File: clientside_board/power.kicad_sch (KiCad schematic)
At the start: 11 parts, among them U3 TPS62160DGK

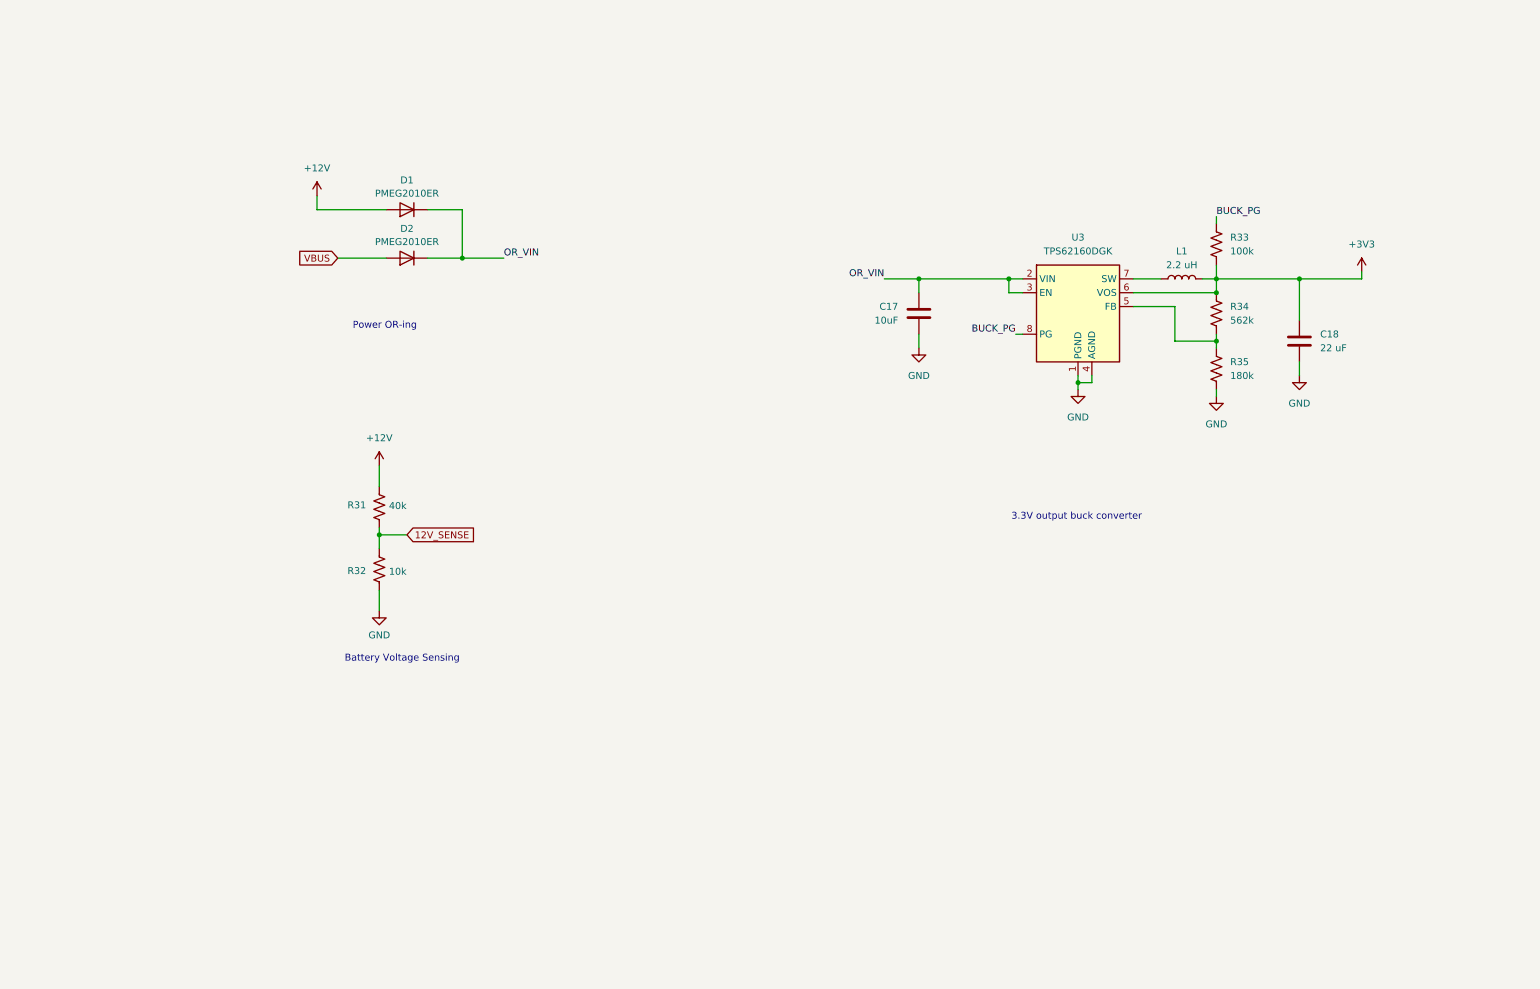
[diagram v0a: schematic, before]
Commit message: Cleanup Power and Ethernet Sheet
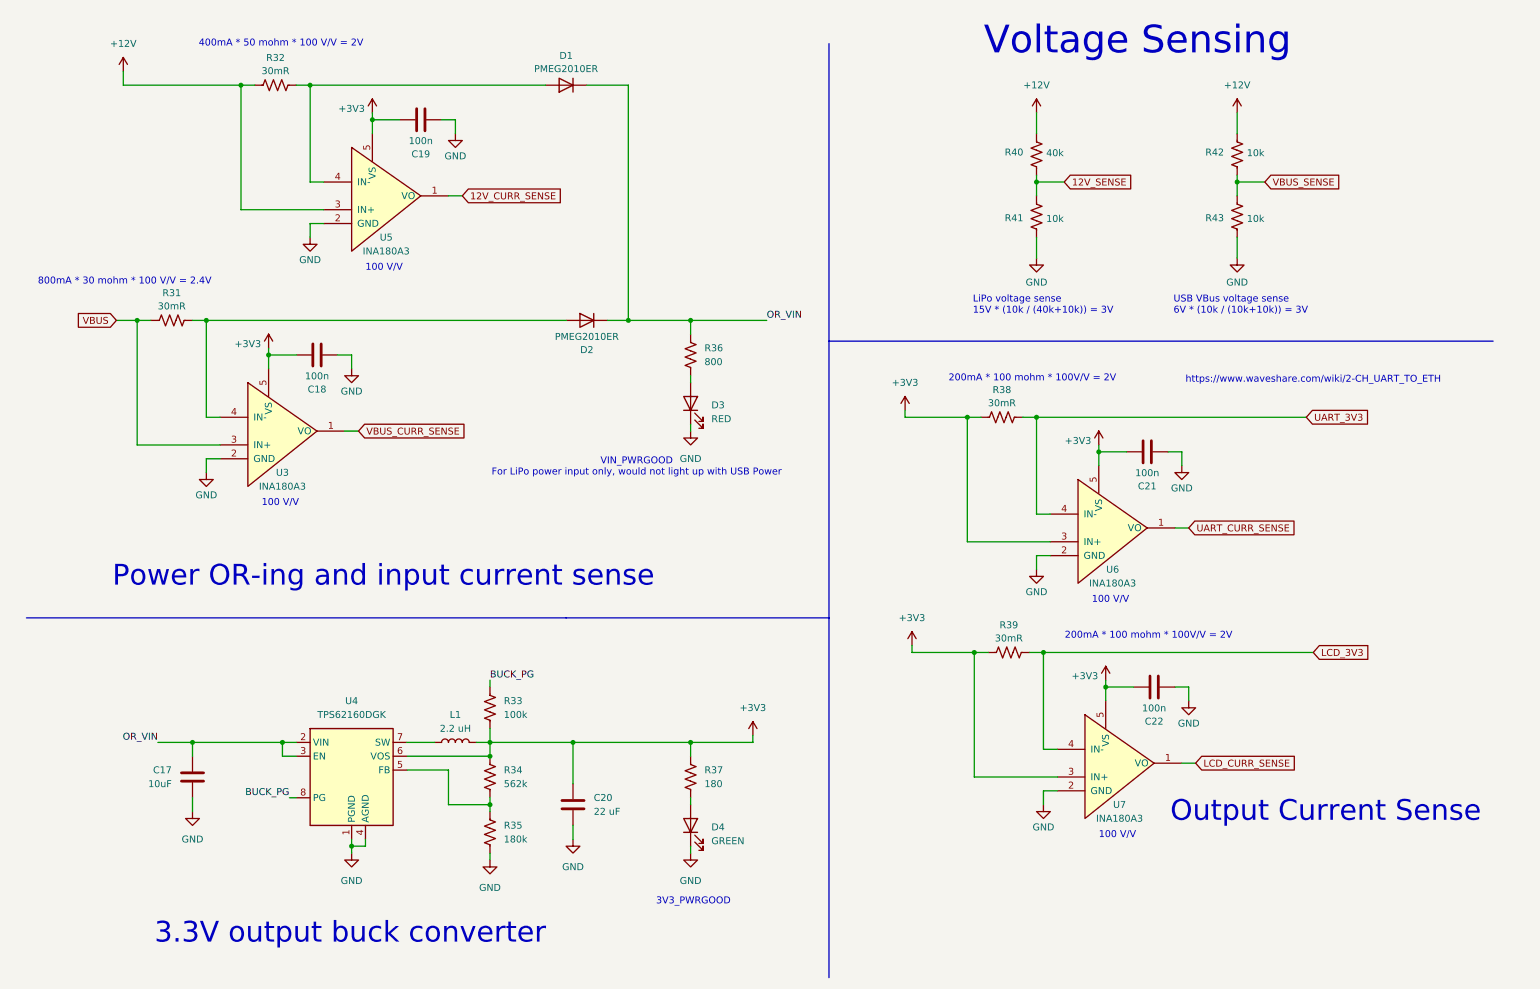
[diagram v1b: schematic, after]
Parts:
- added C18, C19, C21, C22: 100n, Capacitor_SMD:C_0805_2012Metric_Pad1.18x1.45mm_HandSolder, symbol Device:C
- added D3: RED, symbol Device:LED
- added D4: GREEN, symbol Device:LED
- added R31, R32, R38, R39: 30mR, Resistor_SMD:R_0805_2012Metric_Pad1.20x1.40mm_HandSolder, symbol Device:R_US
- added R36: 800, Resistor_SMD:R_0805_2012Metric_Pad1.20x1.40mm_HandSolder, symbol Device:R_US
- added R37: 180, Resistor_SMD:R_0805_2012Metric_Pad1.20x1.40mm_HandSolder, symbol Device:R_US
- added R42, R43: 10k, Resistor_SMD:R_0805_2012Metric_Pad1.20x1.40mm_HandSolder, symbol Device:R_US
- added U3, U5, U6, U7: INA180A3, Package_TO_SOT_SMD:SOT-23-5_HandSoldering, symbol canhw:INA180
- C17: footprint (none) -> Capacitor_SMD:C_0805_2012Metric_Pad1.18x1.45mm_HandSolder
- C20: renamed from C18; footprint (none) -> Capacitor_SMD:C_0805_2012Metric_Pad1.18x1.45mm_HandSolder
- R33, R34, R35: footprint (none) -> Resistor_SMD:R_0805_2012Metric_Pad1.20x1.40mm_HandSolder
- renumbered R31 to R40, R32 to R41, U3 to U4
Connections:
- net +12V: now also R32.1, R42.1, U5.3 (IN+); no longer D1.2 (A)
- net +3V3: now also C18.1, C19.1, C21.1, C22.1, R37.1, R38.1, R39.1, U3.5 (VS), U5.5 (VS), U6.3 (IN+), U6.5 (VS), U7.3 (IN+), U7.5 (VS)
- net GND: now also C18.2, C19.2, C21.2, C22.2, D3.1 (K), D4.1 (K), R43.2, U3.2 (GND), U5.2 (GND), U6.2 (GND), U7.2 (GND)
- net OR_VIN: now also R36.1
- net VBUS: now also R31.1, U3.3 (IN+); no longer D2.2 (A)
- new net: D2.2 (A), R31.2, U3.4 (IN-)
- new net: D3.2 (A), R36.2
- new net: D1.2 (A), R32.2, U5.4 (IN-)
- new net: D4.2 (A), R37.2
- new net 12V_CURR_SENSE: U5.1 (VO)
- new net LCD_3V3: R39.2, U7.4 (IN-)
- new net LCD_CURR_SENSE: U7.1 (VO)
- new net UART_3V3: R38.2, U6.4 (IN-)
- new net UART_CURR_SENSE: U6.1 (VO)
- new net VBUS_CURR_SENSE: U3.1 (VO)
- new net VBUS_SENSE: R42.2, R43.1
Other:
- note added: "100 V/V"
- note added: "200mA * 100 mohm * 100V/V = 2V"
- note added: "3V3_PWRGOOD"
- note added: "400mA * 50 mohm * 100 V/V = 2V"
- note added: "800mA * 30 mohm * 100 V/V = 2.4V"
- note added: "LiPo voltage sense 15V * (10k / (40k+10k)) = 3V"
- note added: "Output Current Sense"
- note added: "Power OR-ing and input current sense"
- note added: "USB VBus voltage sense 6V * (10k / (10k+10k)) = 3V"
- note added: "VIN_PWRGOOD For LiPo power input only, would not light up with USB Power"
- note added: "Voltage Sensing"
- note added: "https://www.waveshare.com/wiki/2-CH_UART_TO_ETH"
- note removed: "Battery Voltage Sensing"
- note removed: "Power OR-ing"
- title: (none) -> Clientside Board Power Conversion and Sensing
- moved on the sheet: C17, C20, D1, D2, L1, R33, R34, R35, R40, R41, U4

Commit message: Start MCU pin connection
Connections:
- net +12V: no longer R42.1
- net VBUS: now also R42.1
- net 12V_SENSE renamed 12V_VOLT_SENSE
- net VBUS_SENSE renamed VBUS_VOLT_SENSE

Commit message: Fix decoupling cap
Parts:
- renumbered C17 to C21, C18 to C22, C19 to C23, C20 to C24, C21 to C25, C22 to C26

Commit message: Integrate new LCD display module
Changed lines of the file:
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@@
 (kicad_sch
-	(version 20231120)
+	(version 20250114)
 	(generator "eeschema")
-	(generator_version "8.0")
+	(generator_version "9.0")
 	(paper "A4")
 	(title_block
@@
 		(date "2025-03-19")
 	)
+	(text "100 V/V"
+		(exclude_from_sim no)
+		(at 76.2 60.96 0)
+		(effects
+			(font
+				(size 1.27 1.27)
+			)
+			(justify left bottom)
+		)
+	)
+	(text "400mA * 50 mohm * 100 V/V = 2V"
+		(exclude_from_sim no)
+		(at 60.706 19.05 0)
+		(effects
+			(font
+				(size 1.27 1.27)
+			)
+		)
+	)
+	(text "VIN_PWRGOOD\nFor LiPo power input only, would not light up with USB Power"
+		(exclude_from_sim no)
+		(at 125.984 96.774 0)
+		(effects
+			(font
+				(size 1.27 1.27)
+			)
+		)
+	)
+	(text "200mA * 100 mohm * 100V/V = 2V"
+		(exclude_from_sim no)
+		(at 198.628 80.518 0)
+		(effects
+			(font
+				(size 1.27 1.27)
+			)
+		)
+	)
+	(text "https://www.waveshare.com/wiki/2-CH_UART_TO_ETH"
+		(exclude_from_sim no)
+		(at 250.19 80.772 0)
+		(effects
+			(font
+				(size 1.27 1.27)
+			)
+		)
+	)
+	(text "Voltage Sensing"
+		(exclude_from_sim no)
+		(at 217.932 18.542 0)
+		(effects
+			(font
+				(size 5.08 5.08)
+			)
+		)
+	)
+	(text "800mA * 30 mohm * 100 V/V = 2.4V"
+		(exclude_from_sim no)
+		(at 32.004 62.738 0)
+		(effects
+			(font
+				(size 1.27 1.27)
+			)
+		)
+	)
+	(text "Power OR-ing and input current sense"
+		(exclude_from_sim no)
+		(at 79.502 116.84 0)
+		(effects
+			(font
+				(size 3.81 3.81)
+			)
+		)
+	)
+	(text "100 V/V"
+		(exclude_from_sim no)
+		(at 210.82 165.1 0)
+		(effects
+			(font
+				(size 1.27 1.27)
+			)
+			(justify left bottom)
+		)
+	)
+	(text "Output Current Sense"
+		(exclude_from_sim no)
+		(at 252.476 160.02 0)
+		(effects
+			(font
+				(size 3.81 3.81)
+			)
+		)
+	)
+	(text "LiPo voltage sense\n15V * (10k / (40k+10k)) = 3V"
+		(exclude_from_sim no)
+		(at 187.706 68.834 0)
+		(effects
+			(font
+				(size 1.27 1.27)
+			)
+			(justify left bottom)
+		)
+	)
+	(text "200mA * 100 mohm * 100V/V = 2V"
+		(exclude_from_sim no)
+		(at 219.964 127.762 0)
+		(effects
+			(font
+				(size 1.27 1.27)
+			)
+		)
+	)
+	(text "100 V/V"
+		(exclude_from_sim no)
+		(at 209.55 121.92 0)
+		(effects
+			(font
+				(size 1.27 1.27)
+			)
+			(justify left bottom)
+		)
+	)
+	(text "3V3_PWRGOOD"
+		(exclude_from_sim no)
+		(at 136.398 176.53 0)
+		(effects
+			(font
+				(size 1.27 1.27)
+			)
+		)
+	)
+	(text "USB VBus voltage sense\n6V * (10k / (10k+10k)) = 3V"
+		(exclude_from_sim no)
+		(at 224.536 68.834 0)
+		(effects
+			(font
+				(size 1.27 1.27)
+			)
+			(justify left bottom)
+		)
+	)
+	(text "100 V/V"
+		(exclude_from_sim no)
+		(at 57.15 104.14 0)
+		(effects
+			(font
+				(size 1.27 1.27)
+			)
+			(justify left bottom)
+		)
+	)
+	(text "3.3V output buck converter"
+		(exclude_from_sim no)
+		(at 73.406 182.372 0)
+		(effects
+			(font
+				(size 3.81 3.81)
+			)
+		)
+	)
 	(junction
 		(at 46.99 69.85)
@@
 		)
 	)
-	(text "100 V/V"
-		(exclude_from_sim no)
-		(at 76.2 60.96 0)
-		(effects
-			(font
-				(size 1.27 1.27)
-			)
-			(justify left bottom)
-		)
-	)
-	(text "400mA * 50 mohm * 100 V/V = 2V"
-		(exclude_from_sim no)
-		(at 60.706 19.05 0)
-		(effects
-			(font
-				(size 1.27 1.27)
-			)
-		)
-	)
-	(text "VIN_PWRGOOD\nFor LiPo power input only, would not light up with USB Power"
-		(exclude_from_sim no)
-		(at 125.984 96.774 0)
-		(effects
-			(font
-				(size 1.27 1.27)
-			)
-		)
-	)
-	(text "200mA * 100 mohm * 100V/V = 2V"
-		(exclude_from_sim no)
-		(at 198.628 80.518 0)
-		(effects
-			(font
-				(size 1.27 1.27)
-			)
-		)
-	)
-	(text "https://www.waveshare.com/wiki/2-CH_UART_TO_ETH"
-		(exclude_from_sim no)
-		(at 250.19 80.772 0)
-		(effects
-			(font
-				(size 1.27 1.27)
-			)
-		)
-	)
-	(text "Voltage Sensing"
-		(exclude_from_sim no)
-		(at 217.932 18.542 0)
-		(effects
-			(font
-				(size 5.08 5.08)
-			)
-		)
-	)
-	(text "800mA * 30 mohm * 100 V/V = 2.4V"
-		(exclude_from_sim no)
-		(at 32.004 62.738 0)
-		(effects
-			(font
-				(size 1.27 1.27)
-			)
-		)
-	)
-	(text "Power OR-ing and input current sense"
-		(exclude_from_sim no)
-		(at 79.502 116.84 0)
-		(effects
-			(font
-				(size 3.81 3.81)
-			)
-		)
-	)
-	(text "100 V/V"
-		(exclude_from_sim no)
-		(at 210.82 165.1 0)
-		(effects
-			(font
-				(size 1.27 1.27)
-			)
-			(justify left bottom)
-		)
-	)
-	(text "Output Current Sense"
-		(exclude_from_sim no)
-		(at 252.476 160.02 0)
-		(effects
-			(font
-				(size 3.81 3.81)
-			)
-		)
-	)
-	(text "LiPo voltage sense\n15V * (10k / (40k+10k)) = 3V"
-		(exclude_from_sim no)
-		(at 187.706 68.834 0)
-		(effects
-			(font
-				(size 1.27 1.27)
-			)
-			(justify left bottom)
-		)
-	)
-	(text "200mA * 100 mohm * 100V/V = 2V"
-		(exclude_from_sim no)
-		(at 219.964 127.762 0)
-		(effects
-			(font
-				(size 1.27 1.27)
-			)
-		)
-	)
-	(text "100 V/V"
-		(exclude_from_sim no)
-		(at 209.55 121.92 0)
-		(effects
-			(font
-				(size 1.27 1.27)
-			)
-			(justify left bottom)
-		)
-	)
-	(text "3V3_PWRGOOD"
-		(exclude_from_sim no)
-		(at 136.398 176.53 0)
-		(effects
-			(font
-				(size 1.27 1.27)
-			)
-		)
-	)
-	(text "USB VBus voltage sense\n6V * (10k / (10k+10k)) = 3V"
-		(exclude_from_sim no)
-		(at 224.536 68.834 0)
-		(effects
-			(font
-				(size 1.27 1.27)
-			)
-			(justify left bottom)
-		)
-	)
-	(text "100 V/V"
-		(exclude_from_sim no)
-		(at 57.15 104.14 0)
-		(effects
-			(font
-				(size 1.27 1.27)
-			)
-			(justify left bottom)
-		)
-	)
-	(text "3.3V output buck converter"
-		(exclude_from_sim no)
-		(at 73.406 182.372 0)
-		(effects
-			(font
-				(size 3.81 3.81)
-			)
-		)
-	)
